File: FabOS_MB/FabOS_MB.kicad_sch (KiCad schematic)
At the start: 8 parts, among them J1 USB_A, J2 USB_C_Receptacle, J3 RJ45, U1 STM32F407VETx, U2 TPS563201, U3 NCV7329, U4 USBLC6-2SC6, U5 HF3F-L 12-1ZL1T

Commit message: Update
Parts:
- added U6: TDPOWER TAS10-12-W2, Librairie_MB:TD POWER TAS12-5-W2, symbol Librairie_MB:Transformateur
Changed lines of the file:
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@@
+		)
+	)
+	(symbol
+		(lib_id "Librairie_MB:Transformateur")
+		(at 176.53 36.83 0)
+		(unit 1)
+		(exclude_from_sim no)
+		(in_bom yes)
+		(on_board yes)
+		(dnp no)
+		(fields_autoplaced yes)
+		(property "Reference" "U6"
+			(at 176.53 24.13 0)
+			(effects
+				(font
+					(size 1.27 1.27)
+				)
+			)
+		)
+		(property "Value" "TDPOWER TAS10-12-W2"
+			(at 176.53 26.67 0)
+			(effects
+				(font
+					(size 1.27 1.27)
+				)
+			)
+		)
+		(property "Footprint" "Librairie_MB:TD POWER TAS12-5-W2"
+			(at 176.53 36.83 0)
+			(effects
+				(font
+					(size 1.27 1.27)
+				)
+				(hide yes)
+			)
+		)
+		(property "Datasheet" "https://www.lcsc.com/datasheet/lcsc_datasheet_2109141830_TDPOWER-TAS10-12-W2_C2687656.pdf"
+			(at 176.53 36.83 0)
+			(effects
+				(font
+					(size 1.27 1.27)
+				)
+				(hide yes)
+			)
+		)
+		(property "Description" "Transformateur vers 12V"
+			(at 176.53 36.83 0)
+			(effects
+				(font
+					(size 1.27 1.27)
+				)
+				(hide yes)
+			)
+		)
+		(property "MPN" "TAS10-12-W2"
+			(at 176.53 36.83 0)
+			(effects
+				(font
+					(size 1.27 1.27)
+				)
+				(hide yes)
+			)
+		)
+		(property "LCSC" " C2687656"
+			(at 176.53 36.83 0)
+			(effects
+				(font
+					(size 1.27 1.27)
+				)
+				(hide yes)
+			)
+		)
+		(pin "1"
+		)
+		(pin "2"
+		)
+		(pin "4"
+		)
+		(pin "6"
+		)
+		(instances
+			(project ""
+				(path "/09377d5d-727f-4ff4-92c8-7a0483d23f1e"
+					(reference "U6")
+					(unit 1)
+				)
+			)
 		)
 	)

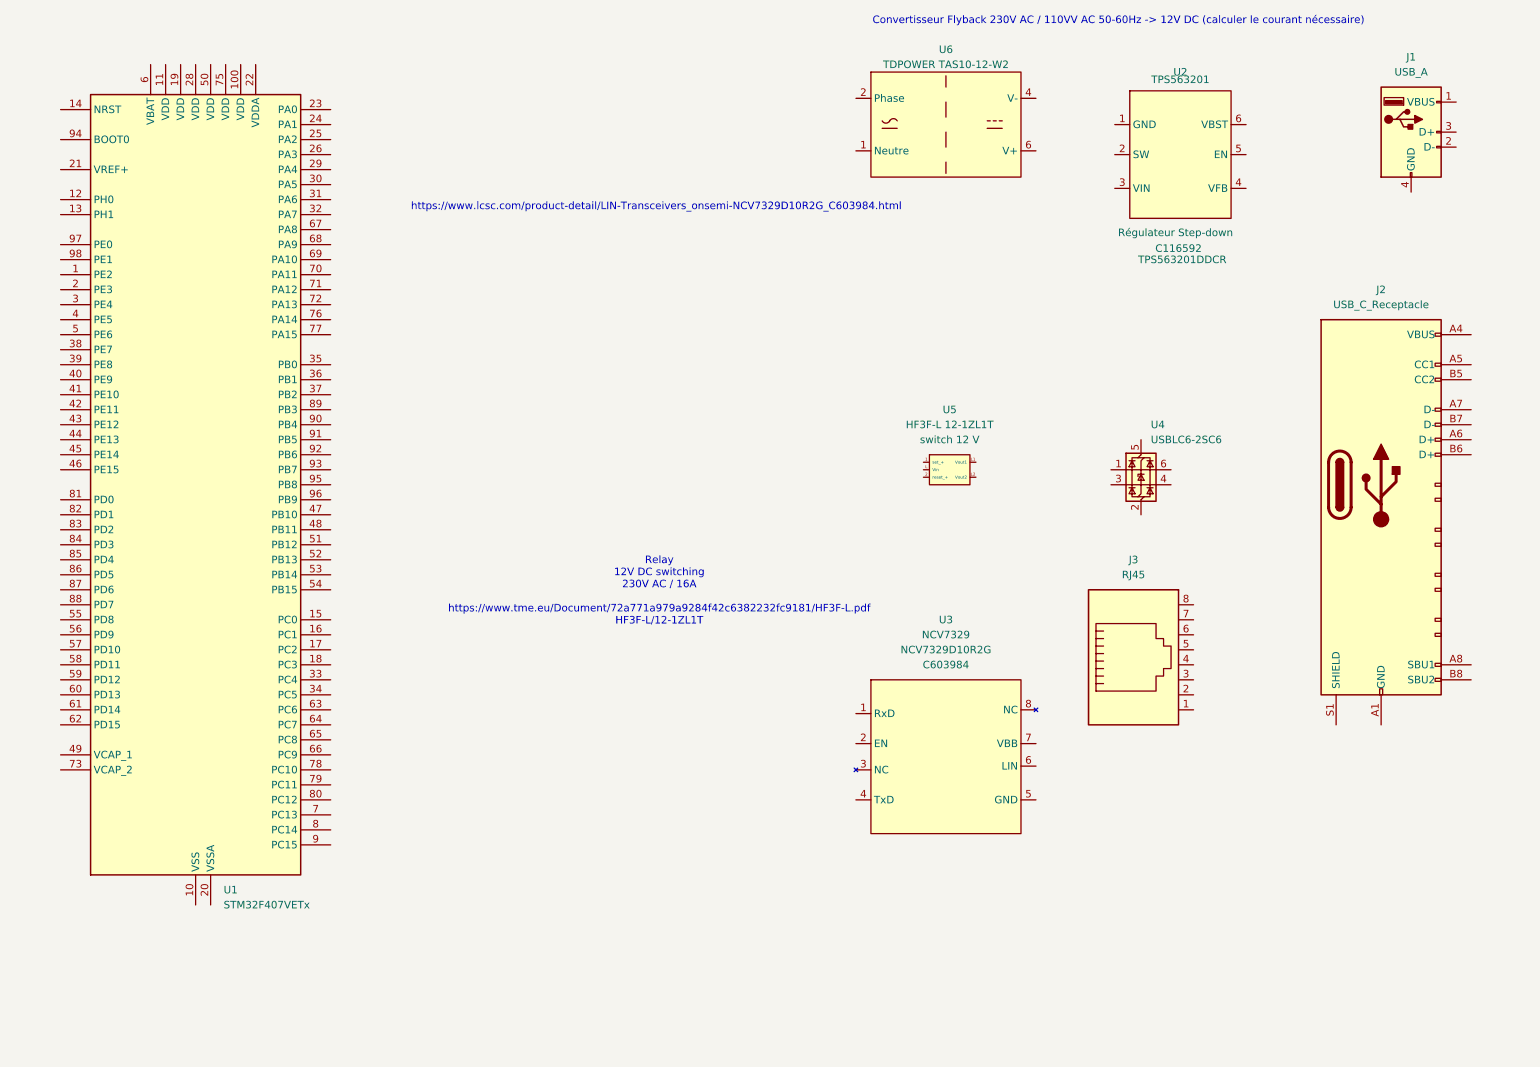
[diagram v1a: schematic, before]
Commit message: Tous les composants ont été posés
Il faut ensuite les relier
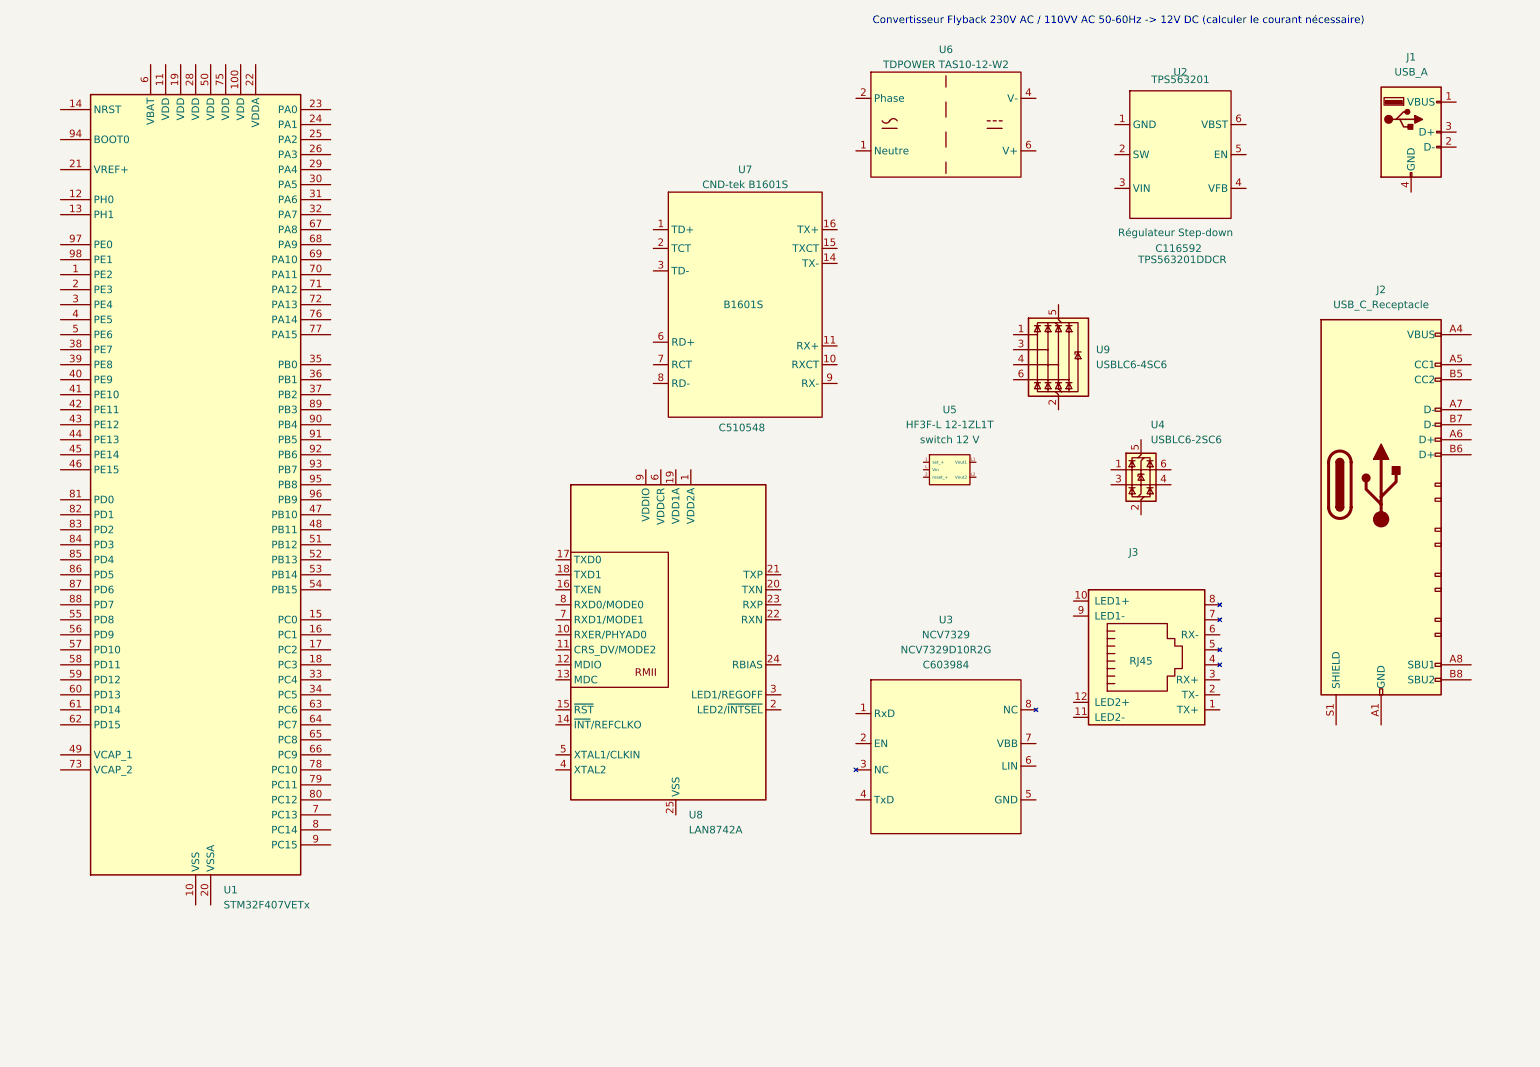
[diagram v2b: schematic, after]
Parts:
- added U7: CND-tek B1601S, Librairie_MB:CND-Tek B1601S, symbol Librairie_MB:CND-tek_B1601S
- added U8: LAN8742A, Package_DFN_QFN:VQFN-24-1EP_4x4mm_P0.5mm_EP2.5x2.5mm_ThermalVias, symbol Interface_Ethernet:LAN8742A
- added U9: USBLC6-4SC6, Package_TO_SOT_SMD:SOT-23-6, symbol Power_Protection:USBLC6-4SC6
- J3: footprint Librairie_MB:RJ_45_Chinois -> Librairie_MB:HC-RJ45-5JAS-1-5-01
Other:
- note removed: "Relay 12V DC switching 230V AC / 16A https://www.tme.eu/Document/72a771a979a9284f42c6382232fc9181/HF3F-L.pdf HF3F-L/12-1ZL1T"
- note removed: "https://www.lcsc.com/product-detail/LIN-Transceivers_onsemi-NCV7329D10R2G_C603984.html"

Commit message: push
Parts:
- removed J3: RJ45, Librairie_MB:HC-RJ45-5JAS-1-5-01, symbol Connector:RJ45
- removed U7: CND-tek B1601S, Librairie_MB:CND-Tek B1601S, symbol Librairie_MB:CND-tek_B1601S
- removed U8: LAN8742A, Package_DFN_QFN:VQFN-24-1EP_4x4mm_P0.5mm_EP2.5x2.5mm_ThermalVias, symbol Interface_Ethernet:LAN8742A
- removed U9: USBLC6-4SC6, Package_TO_SOT_SMD:SOT-23-6, symbol Power_Protection:USBLC6-4SC6
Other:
- added sheet ethernet (ethernet.kicad_sch)

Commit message: feuille usb c
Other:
- added sheet USB_C (usb_c.kicad_sch)
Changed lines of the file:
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@@
+	)
+	(sheet
+		(at 91.44 53.34)
+		(size 62.738 18.034)
+		(fields_autoplaced yes)
+		(stroke
+			(width 0.1524)
+			(type solid)
+		)
+		(fill
+			(color 0 0 0 0.0000)
+		)
+		(property "Sheetname" "USB_C"
+			(at 91.44 52.6284 0)
+			(effects
+				(font
+					(size 1.27 1.27)
+				)
+				(justify left bottom)
+			)
+		)
+		(property "Sheetfile" "usb_c.kicad_sch"
+			(at 91.44 71.9586 0)
+			(effects
+				(font
+					(size 1.27 1.27)
+				)
+				(justify left top)
+			)
+		)
+		(instances
+			(project "FabOS_MB"
+				(path "/09377d5d-727f-4ff4-92c8-7a0483d23f1e"
+					(page "3")
+				)
+			)
+		)
 	)
 	(sheet

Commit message: Sous module USB_C
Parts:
- removed J2: USB_C_Receptacle, Librairie_MB:USB_C_femelle_12P, symbol Connector:USB_C_Receptacle
- removed U4: USBLC6-2SC6, Package_TO_SOT_SMD:SOT-23-6, symbol Power_Protection:USBLC6-2SC6
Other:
- sheet USB_C ports: added USB_BOOT_DM, USB_BOOT_DP, V_USB; removed none
- note added: "Comment gérer boot0 ?"
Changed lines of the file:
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@@
 		(company "ENSEA")
+	)
+	(text "Comment gérer boot0 ?"
+		(exclude_from_sim no)
+		(at 36.83 180.086 0)
+		(effects
+			(font
+				(size 1.27 1.27)
+			)
+		)
 	)
 	(text "Convertisseur Flyback 230V AC / 110VV AC 50-60Hz -> 12V DC (calculer le courant nécessaire)"
@@
 	)
 	(symbol
-		(lib_id "Connector:USB_C_Receptacle")
-		(at 250.19 97.79 0)
-		(unit 1)
-		(exclude_from_sim no)
-		(in_bom yes)
-		(on_board yes)
-		(dnp no)
-		(fields_autoplaced yes)
-		(property "Reference" "J2"
-			(at 250.19 64.77 0)
-			(effects
-				(font
-					(size 1.27 1.27)
-				)
-			)
-		)
-		(property "Value" "USB_C_Receptacle"
-			(at 250.19 67.31 0)
-			(effects
-				(font
-					(size 1.27 1.27)
-				)
-			)
-		)
-		(property "Footprint" "Librairie_MB:USB_C_femelle_12P"
-			(at 254 97.79 0)
-			(effects
-				(font
-					(size 1.27 1.27)
-				)
-				(hide yes)
-			)
-		)
-		(property "Datasheet" "https://www.lcsc.com/datasheet/lcsc_datasheet_2009111836_SOFNG-MC-311D_C136423.pdf"
-			(at 254 97.79 0)
-			(effects
-				(font
-					(size 1.27 1.27)
-				)
-				(hide yes)
-			)
-		)
-		(property "Description" "USB 12P"
-			(at 250.19 97.79 0)
-			(effects
-				(font
-					(size 1.27 1.27)
-				)
-				(hide yes)
-			)
-		)
-		(property "MPN" "MC-311D"
-			(at 250.19 97.79 0)
-			(effects
-				(font
-					(size 1.27 1.27)
-				)
-				(hide yes)
-			)
-		)
-		(property "LCSC" "C136423"
-			(at 250.19 97.79 0)
-			(effects
-				(font
-					(size 1.27 1.27)
-				)
-				(hide yes)
-			)
-		)
-		(pin "S1"
-		)
-		(pin "A5"
-		)
-		(pin "A7"
-		)
-		(pin "B7"
-		)
-		(pin "B5"
-		)
-		(pin "A12"
-		)
-		(pin "A6"
-		)
-		(pin "A9"
-		)
-		(pin "A4"
-		)
-		(pin "B8"
-		)
-		(pin "A8"
-		)
-		(pin "B1"
-		)
-		(pin "B6"
-		)
-		(pin "B12"
-		)
-		(pin "B4"
-		)
-		(pin "B9"
-		)
-		(pin "A1"
-		)
-		(instances
-			(project ""
-				(path "/09377d5d-727f-4ff4-92c8-7a0483d23f1e"
-					(reference "J2")
-					(unit 1)
-				)
-			)
-		)
-	)
-	(symbol
-		(lib_id "Power_Protection:USBLC6-2SC6")
-		(at 209.55 95.25 0)
-		(unit 1)
-		(exclude_from_sim no)
-		(in_bom yes)
-		(on_board yes)
-		(dnp no)
-		(fields_autoplaced yes)
-		(property "Reference" "U4"
-			(at 211.2011 87.63 0)
-			(effects
-				(font
-					(size 1.27 1.27)
-				)
-				(justify left)
-			)
-		)
-		(property "Value" "USBLC6-2SC6"
-			(at 211.2011 90.17 0)
-			(effects
-				(font
-					(size 1.27 1.27)
-				)
-				(justify left)
-			)
-		)
-		(property "Footprint" "Package_TO_SOT_SMD:SOT-23-6"
-			(at 210.82 101.6 0)
-			(effects
-				(font
-					(size 1.27 1.27)
-					(italic yes)
-				)
-				(justify left)
-				(hide yes)
-			)
-		)
-		(property "Datasheet" "https://www.st.com/resource/en/datasheet/usblc6-2.pdf"
-			(at 210.82 103.505 0)
-			(effects
-				(font
-					(size 1.27 1.27)
-				)
-				(justify left)
-				(hide yes)
-			)
-		)
-		(property "Description" "Very low capacitance ESD protection diode, 2 data-line, SOT-23-6"
-			(at 209.55 95.25 0)
-			(effects
-				(font
-					(size 1.27 1.27)
-				)
-				(hide yes)
-			)
-		)
-		(pin "2"
-		)
-		(pin "1"
-		)
-		(pin "4"
-		)
-		(pin "5"
-		)
-		(pin "6"
-		)
-		(pin "3"
-		)
-		(instances
-			(project ""
-				(path "/09377d5d-727f-4ff4-92c8-7a0483d23f1e"
-					(reference "U4")
-					(unit 1)
-				)
-			)
-		)
-	)
-	(symbol
 		(lib_id "Librairie_MB:Switch_12V")
 		(at 177.8 95.25 0)
@@
 	)
 	(sheet
-		(at 91.44 53.34)
-		(size 62.738 18.034)
+		(at 137.922 53.34)
+		(size 16.256 18.034)
 		(fields_autoplaced yes)
 		(stroke
@@
 		)
 		(property "Sheetname" "USB_C"
-			(at 91.44 52.6284 0)
+			(at 137.922 52.6284 0)
 			(effects
 				(font
@@
 		)
 		(property "Sheetfile" "usb_c.kicad_sch"
-			(at 91.44 71.9586 0)
+			(at 137.922 71.9586 0)
 			(effects
 				(font
@@
 			)
 		)
+		(pin "V_USB" input
+			(at 137.922 57.15 180)
+			(effects
+				(font
+					(size 1.27 1.27)
+				)
+				(justify left)
+			)
+		)
+		(pin "USB_BOOT_DM" input
+			(at 154.178 66.04 0)
+			(effects
+				(font
+					(size 1.27 1.27)
+				)
+				(justify right)
+			)
+		)
+		(pin "USB_BOOT_DP" input
+			(at 154.178 63.5 0)
+			(effects
+				(font
+					(size 1.27 1.27)
+				)
+				(justify right)
+			)
+		)

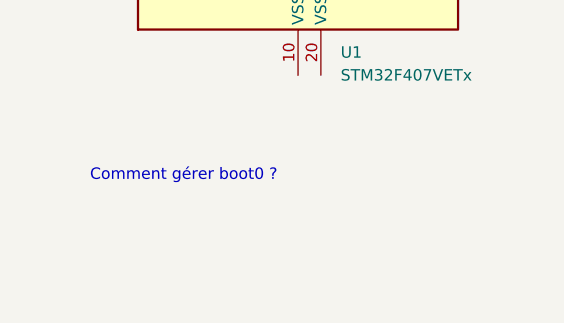
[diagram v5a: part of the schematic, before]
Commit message: Ajout texte
Comment on cable de DFU ? Par OTG ou USART ?
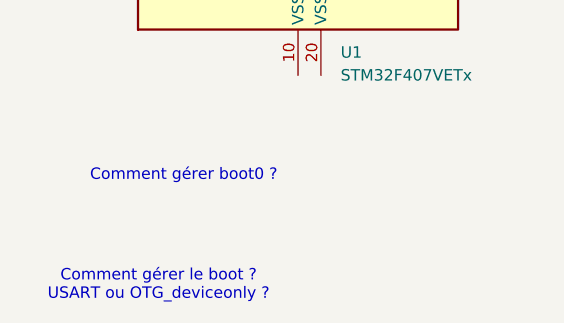
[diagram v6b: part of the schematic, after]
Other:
- note added: "Comment gérer le boot ? USART ou OTG_deviceonly ?"
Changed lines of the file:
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@@
+		)
+	)
+	(text "Comment gérer le boot ?\nUSART ou OTG_deviceonly ?\n"
+		(exclude_from_sim no)
+		(at 34.036 192.278 0)
+		(effects
+			(font
+				(size 1.27 1.27)
+			)
 		)
 	)

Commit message: Pouissance
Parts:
- removed U2: TPS563201, Librairie_MB:TPS563201, symbol Librairie_MB:Step-down_voltage_regulator
- removed U6: TDPOWER TAS10-12-W2, Librairie_MB:TD POWER TAS12-5-W2, symbol Librairie_MB:Transformateur
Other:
- added sheet pouissance (pouissance.kicad_sch)
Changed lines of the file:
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@@
-	)
-	(symbol
-		(lib_id "Librairie_MB:Step-down_voltage_regulator")
-		(at 215.9 41.91 0)
-		(unit 1)
-		(exclude_from_sim no)
-		(in_bom yes)
-		(on_board yes)
-		(dnp no)
-		(property "Reference" "U2"
-			(at 216.2175 27.94 0)
-			(effects
-				(font
-					(size 1.27 1.27)
-				)
-			)
-		)
-		(property "Value" "TPS563201"
-			(at 216.2175 29.21 0)
-			(effects
-				(font
-					(size 1.27 1.27)
-				)
-			)
-		)
-		(property "Footprint" "Librairie_MB:TPS563201"
-			(at 215.265 53.975 0)
-			(effects
-				(font
-					(size 1.27 1.27)
-				)
-				(hide yes)
-			)
-		)
-		(property "Datasheet" "https://www.lcsc.com/datasheet/lcsc_datasheet_2304241919_Texas-Instruments-TPS563201DDCR_C116592.pdf"
-			(at 217.17 55.88 0)
-			(effects
-				(font
-					(size 1.27 1.27)
-				)
-				(hide yes)
-			)
-		)
-		(property "Description" "Régulateur Step-down"
-			(at 215.392 55.118 0)
-			(effects
-				(font
-					(size 1.27 1.27)
-				)
-			)
-		)
-		(property "MPN" "TPS563201DDCR"
-			(at 216.535 59.69 0)
-			(effects
-				(font
-					(size 1.27 1.27)
-				)
-			)
-		)
-		(property "LCSC" "C116592"
-			(at 215.9 57.785 0)
-			(effects
-				(font
-					(size 1.27 1.27)
-				)
-			)
-		)
-		(pin "1"
-		)
-		(pin "2"
-		)
-		(pin "4"
-		)
-		(pin "3"
-		)
-		(pin "5"
-		)
-		(pin "6"
-		)
-		(instances
-			(project ""
-				(path "/09377d5d-727f-4ff4-92c8-7a0483d23f1e"
-					(reference "U2")
-					(unit 1)
-				)
-			)
-		)
 	)
 	(symbol
@@
 		)
 	)
-	(symbol
-		(lib_id "Librairie_MB:Transformateur")
-		(at 176.53 36.83 0)
-		(unit 1)
-		(exclude_from_sim no)
-		(in_bom yes)
-		(on_board yes)
-		(dnp no)
-		(fields_autoplaced yes)
-		(property "Reference" "U6"
-			(at 176.53 24.13 0)
-			(effects
-				(font
-					(size 1.27 1.27)
-				)
-			)
-		)
-		(property "Value" "TDPOWER TAS10-12-W2"
-			(at 176.53 26.67 0)
-			(effects
-				(font
-					(size 1.27 1.27)
-				)
-			)
-		)
-		(property "Footprint" "Librairie_MB:TD POWER TAS12-5-W2"
-			(at 176.53 36.83 0)
-			(effects
-				(font
-					(size 1.27 1.27)
-				)
-				(hide yes)
-			)
-		)
-		(property "Datasheet" "https://www.lcsc.com/datasheet/lcsc_datasheet_2109141830_TDPOWER-TAS10-12-W2_C2687656.pdf"
-			(at 176.53 36.83 0)
-			(effects
-				(font
-					(size 1.27 1.27)
-				)
-				(hide yes)
-			)
-		)
-		(property "Description" "Transformateur vers 12V"
-			(at 176.53 36.83 0)
-			(effects
-				(font
-					(size 1.27 1.27)
-				)
-				(hide yes)
-			)
-		)
-		(property "MPN" "TAS10-12-W2"
-			(at 176.53 36.83 0)
-			(effects
-				(font
-					(size 1.27 1.27)
-				)
-				(hide yes)
-			)
-		)
-		(property "LCSC" " C2687656"
-			(at 176.53 36.83 0)
-			(effects
-				(font
-					(size 1.27 1.27)
-				)
-				(hide yes)
-			)
-		)
-		(pin "1"
-		)
-		(pin "2"
-		)
-		(pin "4"
-		)
-		(pin "6"
-		)
-		(instances
-			(project ""
-				(path "/09377d5d-727f-4ff4-92c8-7a0483d23f1e"
-					(reference "U6")
-					(unit 1)
-				)
-			)
-		)
-	)
 	(sheet
 		(at 137.922 53.34)
@@
 				)
 			)
+		)
+	)
+	(sheet
+		(at 208.026 72.136)
+		(size 47.752 23.368)
+		(fields_autoplaced yes)
+		(stroke
+			(width 0.1524)
+			(type solid)
+		)
+		(fill
+			(color 0 0 0 0.0000)
+		)
+		(property "Sheetname" "pouissance"
+			(at 208.026 71.4244 0)
+			(effects
+				(font
+					(size 1.27 1.27)
+				)
+				(justify left bottom)
+			)
+		)
+		(property "Sheetfile" "pouissance.kicad_sch"
+			(at 208.026 96.0886 0)
+			(effects
+				(font
+					(size 1.27 1.27)
+				)
+				(justify left top)
+			)
+		)
+		(instances
+			(project "FabOS_MB"
+				(path "/09377d5d-727f-4ff4-92c8-7a0483d23f1e"
+					(page "4")
+				)
+			)
